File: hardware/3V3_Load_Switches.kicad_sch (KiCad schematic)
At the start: 28 parts, among them Q18 SI2302DDS-T1-GE3, Q19 SI2302DDS-T1-GE3, Q20 SI2302DDS-T1-GE3, U1 LMV321RIYLT, U2 INA199C3DCKR, U3 INA199C3DCKR, U4 INA199C1DCKR, U5 NVTFS5116PLTAG, U6 NVTFS5116PLTAG, U7 NVTFS5116PLTAG

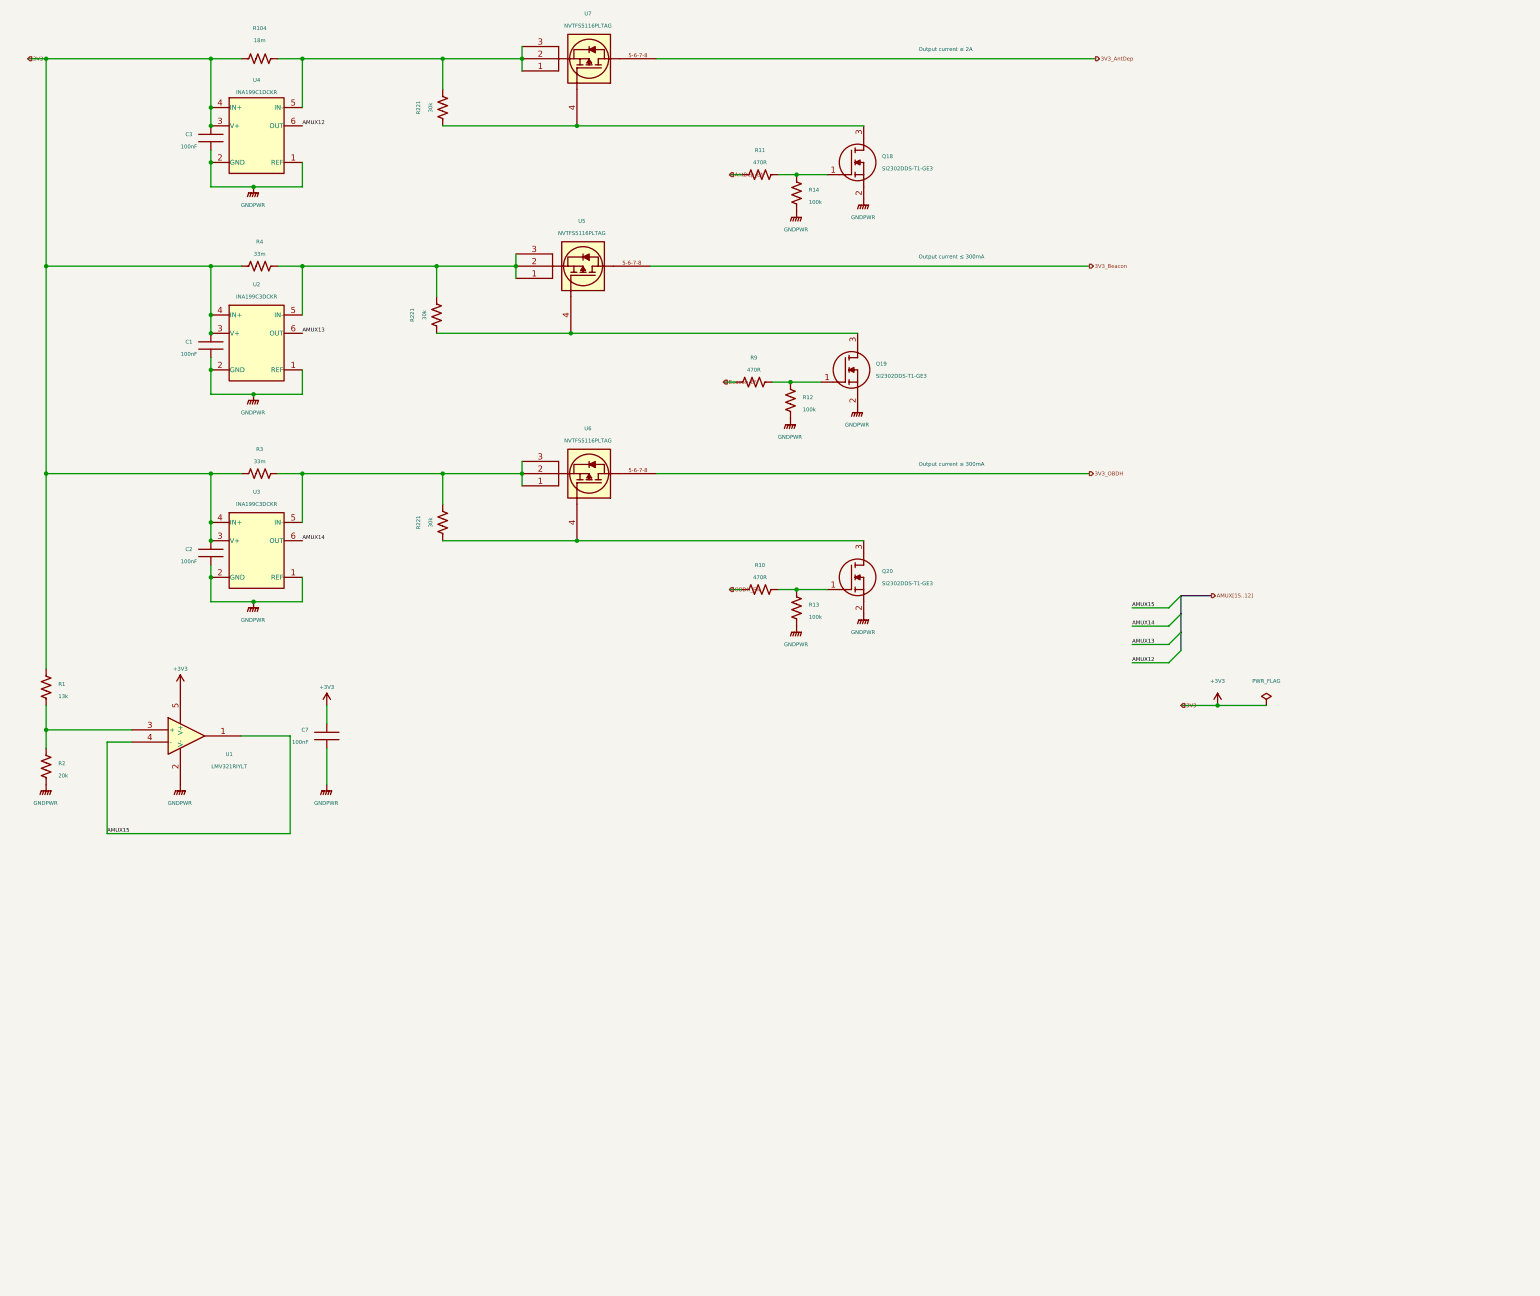
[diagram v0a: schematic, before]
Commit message: hardware: Improving the readability of schematics
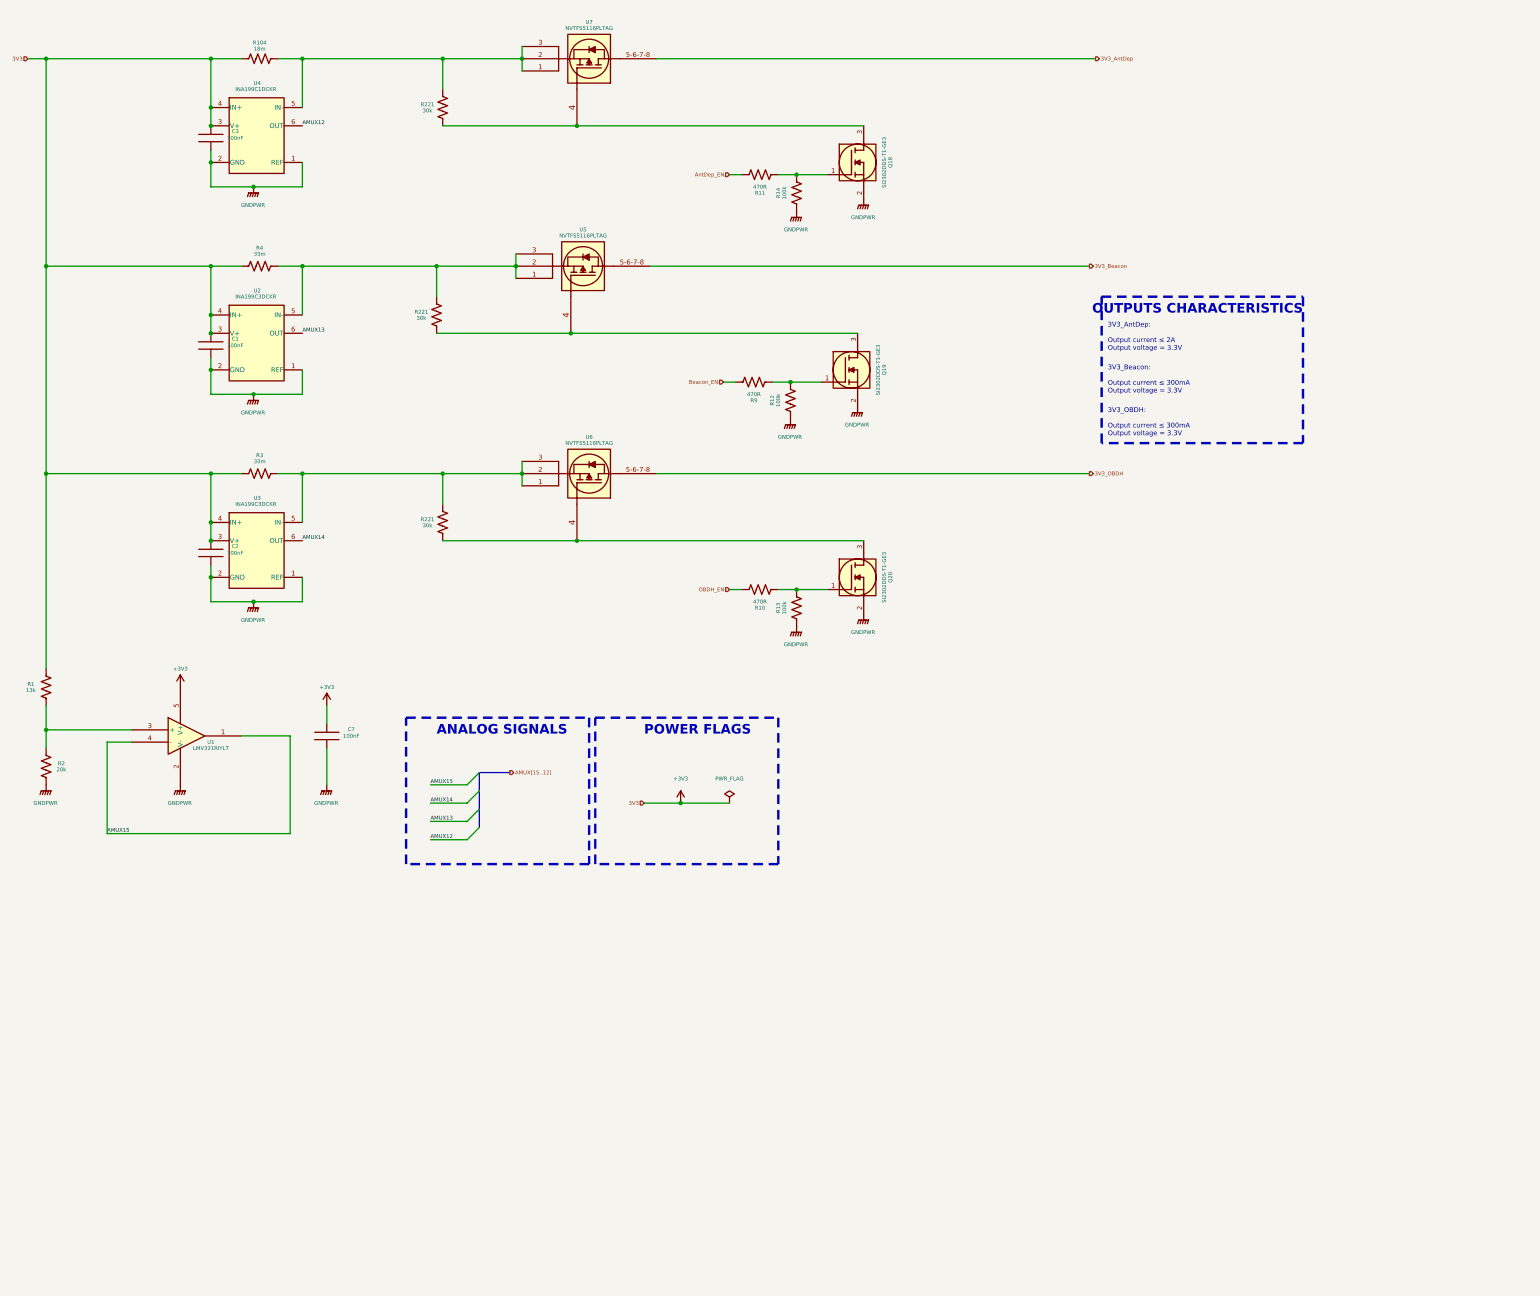
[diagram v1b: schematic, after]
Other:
- note added: "3V3_AntDep: Output current ≤ 2A Output voltage = 3.3V"
- note added: "3V3_Beacon: Output current ≤ 300mA Output voltage = 3.3V"
- note added: "3V3_OBDH: Output current ≤ 300mA Output voltage = 3.3V"
- note added: "ANALOG SIGNALS"
- note added: "OUTPUTS CHARACTERISTICS"
- note added: "POWER FLAGS"
- note removed: "Output current ≤ 2A"
- note removed: "Output current ≤ 300mA"

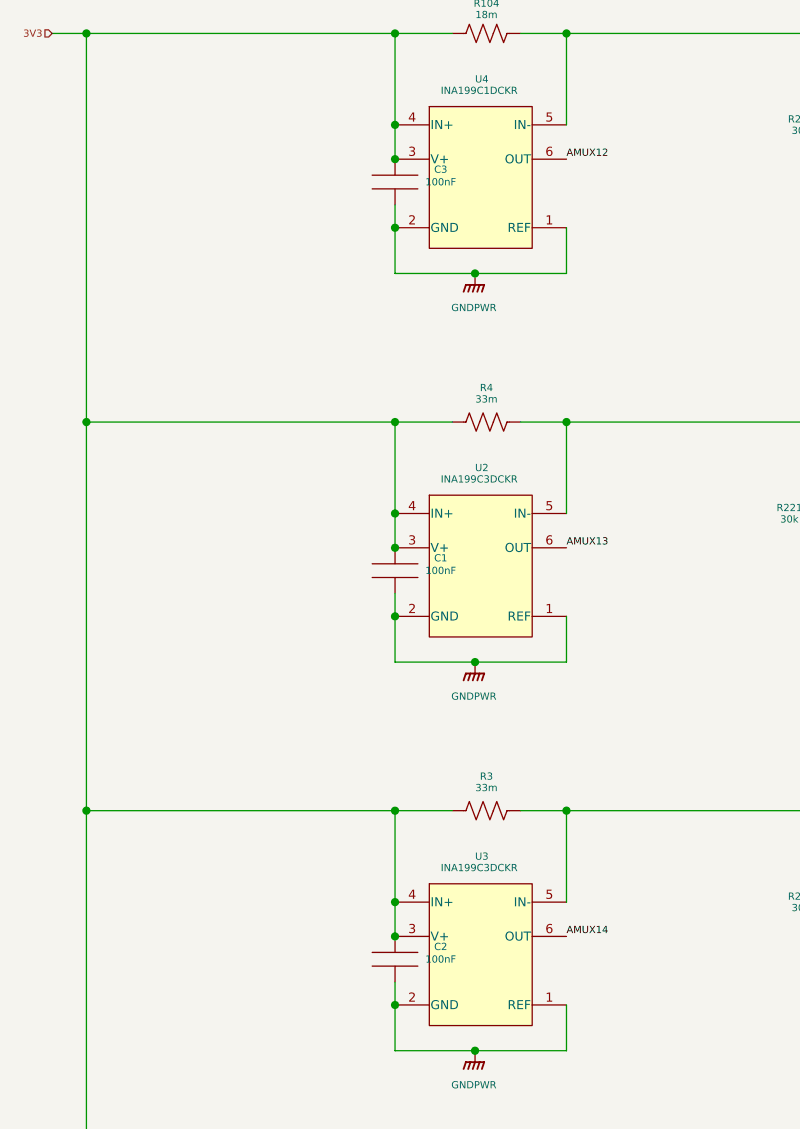
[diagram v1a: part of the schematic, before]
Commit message: hardware: Improving the readability of schematic
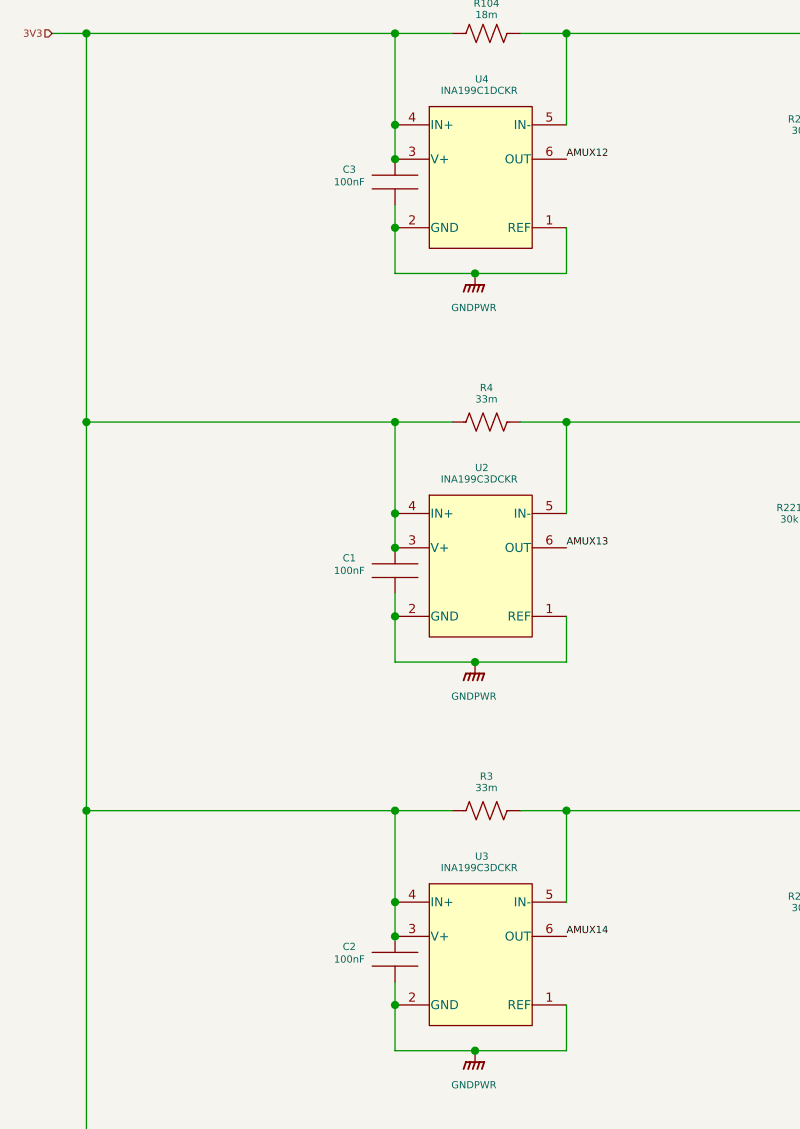
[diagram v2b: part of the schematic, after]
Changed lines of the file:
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@@
   (symbol (lib_id "C0603C104K5RACTU:C0603C104K5RACTU") (at 57.15 129.54 0) (unit 1)
     (in_bom yes) (on_board yes) (dnp no)
-    (property "Reference" "C2" (at 62.23 130.683 0)
-      (effects (font (size 0.8 0.8)))
-    )
-    (property "Value" "100nF" (at 62.23 132.08 0)
+    (property "Reference" "C2" (at 52.07 130.683 0)
+      (effects (font (size 0.8 0.8)))
+    )
+    (property "Value" "100nF" (at 52.07 132.08 0)
       (effects (font (size 0.8 0.8)))
     )
@@
   (symbol (lib_id "C0603C104K5RACTU:C0603C104K5RACTU") (at 57.15 43.18 0) (unit 1)
     (in_bom yes) (on_board yes) (dnp no)
-    (property "Reference" "C3" (at 62.23 44.323 0)
-      (effects (font (size 0.8 0.8)))
-    )
-    (property "Value" "100nF" (at 62.23 45.72 0)
+    (property "Reference" "C3" (at 52.07 44.323 0)
+      (effects (font (size 0.8 0.8)))
+    )
+    (property "Value" "100nF" (at 52.07 45.72 0)
       (effects (font (size 0.8 0.8)))
     )
@@
   (symbol (lib_id "C0603C104K5RACTU:C0603C104K5RACTU") (at 57.15 86.36 0) (unit 1)
     (in_bom yes) (on_board yes) (dnp no)
-    (property "Reference" "C1" (at 62.23 87.503 0)
-      (effects (font (size 0.8 0.8)))
-    )
-    (property "Value" "100nF" (at 62.23 88.9 0)
-      (effects (font (size 0.8 0.8)))
-    )
+    (property "Reference" "C1" (at 52.07 87.503 0)
+      (effects (font (size 0.8 0.8)))
+    )
+    (property "Value" "100nF" (at 52.07 88.9 0)
+      (effects (font (size 0.8 0.8)))
+    )

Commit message: hardware: Making improvements for first release
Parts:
- C1, C2, C3, C7: MPN (none) -> C0603C104K5RACTU; Manufacturer (none) -> KEMET; Package (none) -> SMD 0603; automotive Yes -> (none); automotive grade Grade 1 -> (none); capacitance 0.10 μF -> (none); category Cap -> (none); device class L1 Passive Components -> (none); device class L2 Capacitors -> (none); device class L3 Ceramic Capacitors -> (none); digikey description CAP CER 0.1UF 50V X7R 0603 -> (none); digikey part number 399-5089-2-ND -> (none); height 0.87mm -> (none); lead free Yes -> (none); library id 73022d3323b2b2b8 -> (none); manufacturer KEMET -> (none); material Ceramic -> (none); mouser part number 80-C0603C104K5R7867 -> (none); package 0603 -> (none); rohs Yes -> (none); temperature characteristic X7R -> (none); temperature coefficient 30ppm/°C -> (none); temperature range high +125°C -> (none); temperature range low -55°C -> (none); tolerance 0.1 -> (none); voltage rating 50 V -> (none)
- Q18, Q19, Q20: Height 1.12 -> (none); MPN (none) -> SI2302DDS-T1-GE3; Manufacturer (none) -> Vishay; Manufacturer_Name Vishay -> (none); Manufacturer_Part_Number SI2302DDS-T1-GE3 -> (none); Mouser Part Number 78-SI2302DDS-T1-GE3 -> (none); Mouser Price/Stock https://www.mouser.co.uk/ProductDetail/Vishay-Semiconductor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 -> (none); Package (none) -> SOT-23-3
- R1: MPN (none) -> CRCW060313K0FKEAHP; Manufacturer (none) -> Vishay; Package (none) -> SMD 0603
- R10, R11, R9: MPN (none) -> CRCW0603470RFKEAHP; Manufacturer (none) -> Vishay; Package (none) -> SMD 0603; automotive Yes -> (none); automotive grade Grade 0 -> (none); category Res -> (none); composition Thick Film -> (none); device class L1 Passive Components -> (none); device class L2 Resistors -> (none); device class L3 Chip SMD Resistors -> (none); height 0.55mm -> (none); ipc land pattern name RESC16085X45 -> (none); lead free Yes -> (none); library id 3843bba7e74bf2ed -> (none); manufacturer Vishay -> (none); package 0603 -> (none); power 250mW -> (none); power rating 0.33W -> (none); resistance 470Ω -> (none); rohs Yes -> (none); series CRCW-HP e3 -> (none); temperature coefficient 100ppm/°C -> (none); temperature range high +155°C -> (none); temperature range low -55°C -> (none); tolerance 1% -> (none); voltage rating 75V -> (none)
- R104: Height 0.889 -> (none); MPN (none) -> WSL2010R0180FEA; Manufacturer (none) -> Vishay; Manufacturer_Name Vishay -> (none); Manufacturer_Part_Number WSL2010R0180FEA -> (none); Mouser Part Number 71-WSL2010R0180FEA -> (none); Mouser Price/Stock https://www.mouser.co.uk/ProductDetail/Vishay-Dale/WSL2010R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 -> (none); Package (none) -> SMD 2010
- R12, R13, R14: Arrow Part Number CRCW0603100KFKEAHP -> (none); Arrow Price/Stock https://www.arrow.com/en/products/crcw0603100kfkeahp/vishay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 -> (none); Height 0.55 -> (none); MPN (none) -> CRCW0603100KFKEAHP; Manufacturer (none) -> Vishay; Manufacturer_Name Vishay -> (none); Manufacturer_Part_Number CRCW0603100KFKEAHP -> (none); Mouser Part Number 71-CRCW0603100KFKEAH -> (none); Mouser Price/Stock https://www.mouser.co.uk/ProductDetail/Vishay-Dale/CRCW0603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 -> (none); Package (none) -> SMD 0603
- R2: MPN (none) -> CRCW060320K0FKEAHP; Manufacturer (none) -> Vishay; Package (none) -> SMD 0603; automotive Yes -> (none); automotive grade Grade 0 -> (none); category Res -> (none); composition Thick Film -> (none); device class L1 Passive Components -> (none); device class L2 Resistors -> (none); device class L3 Chip SMD Resistors -> (none); height 0.55mm -> (none); ipc land pattern name RESC16085X45 -> (none); lead free Yes -> (none); library id 6d0e00b833a89e4b -> (none); manufacturer Vishay -> (none); package 0603 -> (none); power 250mW -> (none); power rating 0.33W -> (none); resistance 20kΩ -> (none); rohs Yes -> (none); series CRCW-HP e3 -> (none); temperature coefficient 100ppm/°C -> (none); temperature range high +155°C -> (none); temperature range low -55°C -> (none); tolerance 1% -> (none); voltage rating 75V -> (none)
- R221: MPN (none) -> CRCW060330K0FKEAHP; Manufacturer (none) -> Vishay; Package (none) -> SMD 0603
- R3, R4: MPN (none) -> WSL2010R0330FEA; Manufacturer (none) -> Vishay; Package (none) -> SMD 2010
- U1: MPN (none) -> LMV321RIYLT; Manufacturer (none) -> STMicroelectronics; Package (none) -> SOT-23-5
- U2, U3: footprint Package_TO_SOT_SMD:SOT-363_SC-70-6 -> footprints:INA199C3DCKR; symbol INA199C3DCKR:INA199xxDCK -> INA199C3DCKR:INA199C3DCKR; MPN (none) -> INA199C3DCKR; Manufacturer (none) -> TI; Package (none) -> SC70-6
- U4: symbol INA199C1DCKR:INA199xxDCK -> INA199C1DCKR:INA199C1DCKR; MPN (none) -> INA199C1DCKR; Manufacturer (none) -> TI; Package (none) -> SC70-6
- U5, U6, U7: MPN (none) -> NVTFS5116PLTAG; Manufacturer (none) -> onsemi; Package (none) -> WDFN-8
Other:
- moved on the sheet: U2, U3, U4

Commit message: hardware: Minor improvements to the schematics
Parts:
- U4: footprint footprints:INA199C1DCKR -> footprints:INA199C1DCKR
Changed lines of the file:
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@@
       (effects (font (size 0.8 0.8)))
     )
-    (property "Footprint" "footprints:INA199C1DCKR " (at 66.04 55.88 0)
+    (property "Footprint" "footprints:INA199C1DCKR" (at 66.04 55.88 0)
       (effects (font (size 1.27 1.27)) hide)
     )
-    (property "Datasheet" "http://www.ti.com/lit/ds/symlink/ina199.pdf" (at 72.39 58.42 0)
+    (property "Datasheet" "https://www.ti.com/lit/ds/symlink/ina199.pdf?HQS=dis-mous-null-mousermode-dsf-pf-null-wwe&ts=1699134415152" (at 72.39 58.42 0)
       (effects (font (size 1.27 1.27)) hide)
     )

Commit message: hardware: update schematic and layout projects
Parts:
- R6, R7, R8: renamed from R221; symbol CRCW060330K0FKEAHP:RES -> CRCW060330K0FKEAHP:CRCW060330K0FKEAHP
- U4: Manufacturer TI -> Texas Instruments
- renumbered R104 to R5
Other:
- note removed: "ANALOG SIGNALS"
- note removed: "OUTPUTS CHARACTERISTICS"
- note removed: "POWER FLAGS"
- moved on the sheet: C1, C2, C3, C7, Q18, Q19, Q20, R1, R10, R11, R12, R13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
